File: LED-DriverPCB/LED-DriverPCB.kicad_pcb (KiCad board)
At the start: 4 copper layers, 246 x 144.3 mm, 51 parts, among them J1 Screw_Terminal_01x03, J12 Screw_Terminal_01x02, J13 Screw_Terminal_01x02, J14 Screw_Terminal_01x02, J15 Screw_Terminal_01x02, J16 Screw_Terminal_01x02, J17 Screw_Terminal_01x02, J18 Screw_Terminal_01x02, J19 Screw_Terminal_01x02, J2 Screw_Terminal_01x03, J20 Conn_ARM_SWD_TagConnect_TC2030, J3 Screw_Terminal_01x03, J4 Screw_Terminal_01x03, J5 Screw_Terminal_01x03, J6 Screw_Terminal_01x03, J7 Screw_Terminal_01x03, J8 Screw_Terminal_01x03, J9 USB_C_Receptacle_USB2.0_16P, U1 STM32F103RCTx, U2 TXB0108PW, U3 AMS1117-3.3, U4 USBLC6-2SC6, X1 8MHz

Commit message: Finalized layout
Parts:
- C1, C2: value C -> 10p
- moved J12 3.25 mm to (121.2, 99.0)
- moved J13 3.25 mm to (121.2, 111.6)
- moved J14 3.25 mm to (121.2, 124.2)
- moved J15 3.25 mm to (121.2, 136.8)
- moved J16 3.25 mm to (121.2, 149.5)
- moved J17 3.25 mm to (121.2, 162.1)
- moved J18 3.25 mm to (121.2, 174.7)
- moved J19 3.25 mm to (121.2, 187.3)
- moved J1 2.86 mm to (323.3, 200.1)
- moved J2 2.86 mm to (302.1, 200.1)
- moved J3 2.86 mm to (280.9, 200.1)
- moved J4 2.86 mm to (259.6, 200.1)
- moved J5 2.86 mm to (205.7, 200.1)
- moved J6 2.86 mm to (184.5, 200.1)
- moved J7 2.86 mm to (163.3, 200.1)
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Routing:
- net /STR6_PWR: track 100.1 -> 94.0 mm
- net /STR5_PWR: track 124.3 -> 118.2 mm
- net /STR4_PWR: track 178.6 -> 172.5 mm
- net /STR8_PWR: track 33.0 -> 26.8 mm
- net /STR7_PWR: track 66.7 -> 60.6 mm
- net /STR2_PWR: track 270.6 -> 264.5 mm
- net /STR3_PWR: track 240.6 -> 234.6 mm
- net /STR1_PWR: track 300.6 -> 294.6 mm
- net /STR8_DATA: track 130.6 -> 127.7 mm
- net /STR7_DATA: track 110.1 -> 107.2 mm
- net /STR6_DATA: track 89.5 -> 86.6 mm
- net /STR5_DATA: track 68.9 -> 66.0 mm
- net /STR4_DATA: track 69.4 -> 66.6 mm
- net /STR3_DATA: track 90.2 -> 87.3 mm
- net /STR2_DATA: track 110.8 -> 108.0 mm
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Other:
- board size 246 x 144.3 mm -> 244 x 142.3 mm
- board text added: "GND"
- board text added: "POWER 1"
- board text added: "POWER 2"
- board text added: "POWER 3"
- board text added: "POWER 4"
- board text added: "POWER 5"
- board text added: "POWER 6"
- board text added: "POWER 7"
- board text added: "POWER 8"
- board text added: "PWR"
- board text added: "STRIP 1"
- board text added: "STRIP 2"
- board text added: "STRIP 3"
- board text added: "STRIP 4"
- board text added: "STRIP 5"
- board text added: "STRIP 6"
- board text added: "STRIP 7"
- board text added: "STRIP 8"

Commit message: Finished PCB
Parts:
- added D1: LED, LED_SMD:LED_0603_1608Metric, F.Cu at (246.5, 143.1)
- added R6: 1k, Resistor_SMD:R_0402_1005Metric, F.Cu at (246.2, 144.7)
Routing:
- net +3.3V: track 114.8 -> 125.1 mm
- net Net-(D1-K): track 0.00 -> 1.61 mm
- net GND: track 49.7 -> 50.5 mm, vias 63 -> 62
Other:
- board text added: "06/25"
- board text added: "REV A"
- board text added: "Tim Short's Garage"
- board text added: "timshortsgarage.ca"

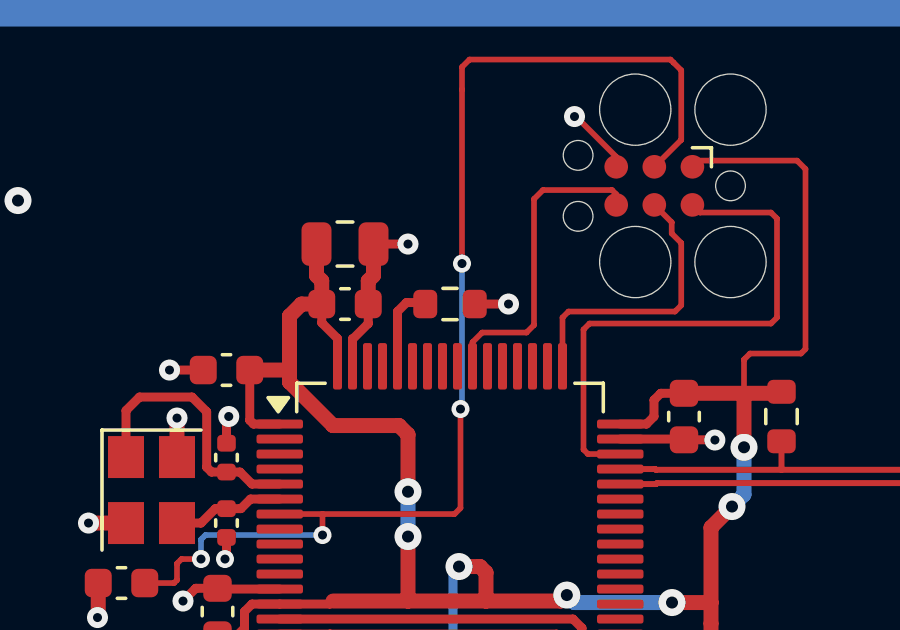
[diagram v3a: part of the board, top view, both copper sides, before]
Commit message: Changed MCU and level shifter
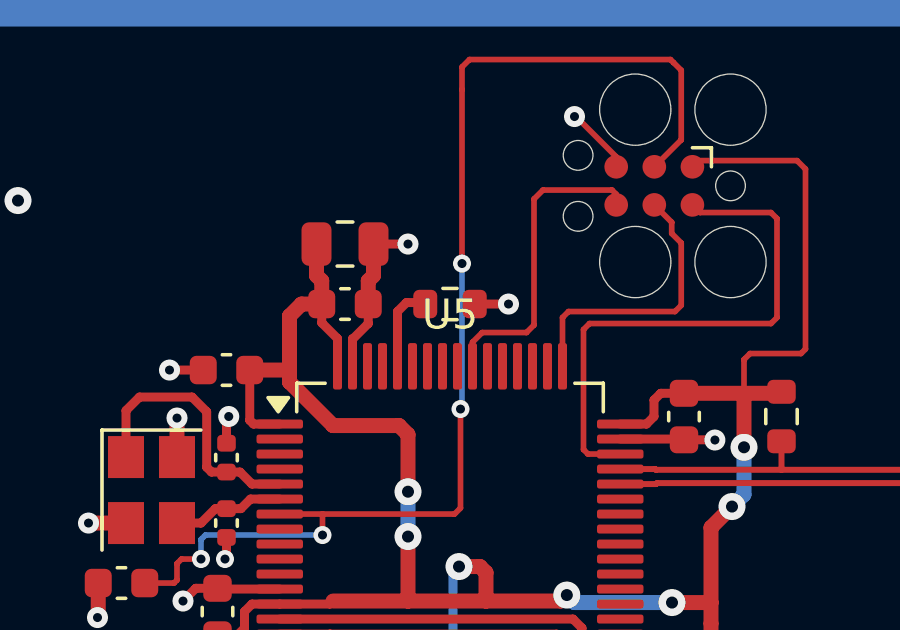
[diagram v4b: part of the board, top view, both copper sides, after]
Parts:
- removed U1: STM32F103RCTx, Package_QFP:LQFP-64_10x10mm_P0.5mm
- added U5: STM32F103RGTx, Package_QFP:LQFP-64_10x10mm_P0.5mm, F.Cu at (228.0, 139.5)

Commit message: fixed bugs
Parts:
- removed C13, C14: 100n, Capacitor_SMD:C_0603_1608Metric
- removed C15: 10u, Capacitor_SMD:C_0805_2012Metric
- removed U2: TXB0108PW, Package_SO:TSSOP-20_4.4x6.5mm_P0.65mm
- added C16: 100n, Capacitor_SMD:C_0603_1608Metric, F.Cu at (231.6, 152.0)
- added G***: LOGO, LOGO, F.Cu at (240.9, 104.2)
- added G***: LOGO, LOGO, F.Cu at (275.3, 114.9)
- added R10: 0R, Resistor_SMD:R_0603_1608Metric, F.Cu at (234.9, 157.7)
- added R11: 0R, Resistor_SMD:R_0603_1608Metric, F.Cu at (234.9, 159.5)
- added R12: 0R, Resistor_SMD:R_0603_1608Metric, F.Cu at (221.2, 154.0)
- added R13: 0R, Resistor_SMD:R_0603_1608Metric, F.Cu at (221.2, 155.8)
- added R14: 0R, Resistor_SMD:R_0603_1608Metric, F.Cu at (221.2, 157.7)
- added R15: 0R, Resistor_SMD:R_0603_1608Metric, F.Cu at (221.2, 159.5)
- added R7: 10k, Resistor_SMD:R_0603_1608Metric, F.Cu at (234.9, 152.1)
- added R8: 0R, Resistor_SMD:R_0603_1608Metric, F.Cu at (234.9, 154.0)
- added R9: 0R, Resistor_SMD:R_0603_1608Metric, F.Cu at (234.9, 155.8)
- added TP1: TestPoint, TestPoint:TestPoint_Pad_1.0x1.0mm, F.Cu at (216.9, 154.0)
- added TP2: TestPoint, TestPoint:TestPoint_Pad_1.0x1.0mm, F.Cu at (213.7, 155.8)
- added TP3: TestPoint, TestPoint:TestPoint_Pad_1.0x1.0mm, F.Cu at (210.4, 157.7)
- added TP4: TestPoint, TestPoint:TestPoint_Pad_1.0x1.0mm, F.Cu at (207.2, 159.5)
- added TP5: TestPoint, TestPoint:TestPoint_Pad_1.0x1.0mm, F.Cu at (248.1, 159.5)
- added TP6: TestPoint, TestPoint:TestPoint_Pad_1.0x1.0mm, F.Cu at (251.5, 157.7)
- added TP7: TestPoint, TestPoint:TestPoint_Pad_1.0x1.0mm, F.Cu at (254.9, 155.8)
- added TP8: TestPoint, TestPoint:TestPoint_Pad_1.0x1.0mm, F.Cu at (258.2, 154.0)
- added U1: 74AHCT244, Package_SO:TSSOP-20_4.4x6.5mm_P0.65mm, F.Cu at (228.0, 156.4)
- R4: value 50k -> 10k
- moved R4 3.28 mm to (221.2, 152.1), turned to 180 degrees
- moved C8 0.95 mm to (219.3, 142.0)
- moved C10 0.83 mm to (216.3, 141.0)
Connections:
- R4 pad 1: +3.3V -> Net-(U1-1OE)
- R4 pad 2: /SHIFTER_OE -> GND
- U5 pad 25: /PWM_TIM8_CH1 -> unconnected-(U5-PC5-Pad25)
- U5 pad 37: unconnected-(U5-PC6-Pad37) -> /PWM_TIM8_CH1
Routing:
- net VBUS: track 160.2 -> 137.5 mm
- net +3.3V: track 125.1 -> 108.2 mm, vias 10 -> 9
- net /PWM_TIM8_CH1: track 10.3 -> 24.7 mm, vias 0 -> 2
- net /STR5_DATA: track 66.0 -> 59.2 mm
- net /STR4_DATA: track 66.6 -> 60.0 mm
- net /PWM_TIM5_CH1: track 26.1 -> 19.8 mm
- net /PWM_TIM3_CH1: track 12.3 -> 17.5 mm, vias 2 -> 0
- net /PWM_TIM5_CH2: track 25.3 -> 20.1 mm
- net /PWM_TIM5_CH4: track 17.7 -> 22.7 mm, vias 2 -> 0
- net Net-(U1-2OE): track 0.00 -> 4.62 mm
- net /STR6_DATA: track 86.6 -> 82.3 mm
- net Net-(U1-1OE): track 0.00 -> 4.26 mm
- net /STR3_DATA: track 87.3 -> 83.1 mm
- net /PWM_TIM3_CH3: track 9.18 -> 13.4 mm, vias 2 -> 0
- net /2Y3_RES: track 0.00 -> 3.50 mm
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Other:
- board text added: "07/25"
- board text added: "REV B"
- board text removed: "06/25"
- board text removed: "REV A"

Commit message: Small changes
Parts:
- added G***: LOGO, LOGO, F.Cu at (205.7, 131.7)
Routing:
- net +3.3V: track 108.2 -> 109.6 mm

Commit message: Fixed issues
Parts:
- moved TP1 41.3 mm to (216.9, 154.0)
- moved TP8 41.3 mm to (258.2, 154.0)
- moved TP2 41.2 mm to (213.7, 155.8)
- moved TP7 41.2 mm to (254.9, 155.8)
- moved TP3 41.1 mm to (210.4, 157.7)
- moved TP6 41.1 mm to (251.5, 157.7)
- moved TP4 40.9 mm to (207.2, 159.5)
- moved TP5 40.9 mm to (248.1, 159.5)
- renumbered TP8 to TP1, TP7 to TP2, TP6 to TP3, TP5 to TP4, TP4 to TP5, TP3 to TP6, TP2 to TP7, TP1 to TP8
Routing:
- net VBUS: track 137.5 -> 146.1 mm
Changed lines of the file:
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@@
 			)
 		)
+		(property "JLCPCB Part #" "C21189"
+			(at 0 0 0)
+			(unlocked yes)
+			(layer "F.Fab")
+			(hide yes)
+			(effects
+				(font
+					(size 1 1)
+					(thickness 0.15)
+				)
+			)
+		)
 		(property ki_fp_filters "R_*")
 		(sheetname "/")
@@
 			)
 		)
+		(property "JLCPCB Part #" " C25804"
+			(at 0 0 180)
+			(unlocked yes)
+			(layer "F.Fab")
+			(hide yes)
+			(effects
+				(font
+					(size 1 1)
+					(thickness 0.15)
+				)
+			)
+		)
 		(property ki_fp_filters "R_*")
 		(sheetname "/")
@@
 			)
 		)
+		(property "JLCPCB Part #" "C484743"
+			(at 0 0 0)
+			(unlocked yes)
+			(layer "F.Fab")
+			(hide yes)
+			(effects
+				(font
+					(size 1 1)
+					(thickness 0.15)
+				)
+			)
+		)
 		(property ki_fp_filters "TSSOP*4.4x6.5mm*P0.65mm* SSOP*4.4x6.5mm*P0.65mm*")
 		(sheetname "/")
@@
 			)
 		)
+		(property "JLCPCB Part #" "C21189"
+			(at 0 0 180)
+			(unlocked yes)
+			(layer "F.Fab")
+			(hide yes)
+			(effects
+				(font
+					(size 1 1)
+					(thickness 0.15)
+				)
+			)
+		)
 		(property ki_fp_filters "R_*")
 		(sheetname "/")
@@
 	(footprint "TestPoint:TestPoint_Pad_1.0x1.0mm"
 		(layer "F.Cu")
-		(at 216.879 153.959)
+		(at 258.229 153.959)
 		(descr "SMD rectangular pad as test Point, square 1.0mm side length")
 		(tags "test point SMD pad rectangle square")
-		(property "Reference" "TP1"
+		(property "Reference" "TP8"
 			(at -2.85 -0.925 0)
 			(layer "F.SilkS")
@@
 	(footprint "TestPoint:TestPoint_Pad_1.0x1.0mm"
 		(layer "F.Cu")
-		(at 251.495667 157.659)
+		(at 210.445667 157.659)
 		(descr "SMD rectangular pad as test Point, square 1.0mm side length")
 		(tags "test point SMD pad rectangle square")
-		(property "Reference" "TP6"
+		(property "Reference" "TP3"
 			(at -2.733333 -0.833333 0)
 			(layer "F.SilkS")
@@
 			)
 		)
+		(property "JLCPCB Part #" "C21189"
+			(at 0 0 180)
+			(unlocked yes)
+			(layer "F.Fab")
+			(hide yes)
+			(effects
+				(font
+					(size 1 1)
+					(thickness 0.15)
+				)
+			)
+		)
 		(property ki_fp_filters "R_*")
 		(sheetname "/")
@@
 	(footprint "TestPoint:TestPoint_Pad_1.0x1.0mm"
 		(layer "F.Cu")
-		(at 213.662333 155.809)
+		(at 254.862333 155.809)
 		(descr "SMD rectangular pad as test Point, square 1.0mm side length")
 		(tags "test point SMD pad rectangle square")
-		(property "Reference" "TP2"
+		(property "Reference" "TP7"
 			(at -2.833333 -0.908333 0)
 			(layer "F.SilkS")
@@
 			)
 		)
+		(property "JLCPCB Part #" "C21189"
+			(at 0 0 0)
+			(unlocked yes)
+			(layer "F.Fab")
+			(hide yes)
+			(effects
+				(font
+					(size 1 1)
+					(thickness 0.15)
+				)
+			)
+		)
 		(property ki_fp_filters "R_*")
 		(sheetname "/")
@@
 			)
 		)
+		(property "JLCPCB Part #" "C21189"
+			(at 0 0 180)
+			(unlocked yes)
+			(layer "F.Fab")
+			(hide yes)
+			(effects
+				(font
+					(size 1 1)
+					(thickness 0.15)
+				)
+			)
+		)
 		(property ki_fp_filters "R_*")
 		(sheetname "/")
@@
 	(footprint "TestPoint:TestPoint_Pad_1.0x1.0mm"
 		(layer "F.Cu")
-		(at 258.229 153.959)
+		(at 216.879 153.959)
 		(descr "SMD rectangular pad as test Point, square 1.0mm side length")
 		(tags "test point SMD pad rectangle square")
-		(property "Reference" "TP8"
+		(property "Reference" "TP1"
 			(at -2.8 -0.85 0)
 			(layer "F.SilkS")
@@
 			)
 		)
+		(property "JLCPCB Part #" " C25804"
+			(at 0 0 0)
+			(unlocked yes)
+			(layer "F.Fab")
+			(hide yes)
+			(effects
+				(font
+					(size 1 1)
+					(thickness 0.15)
+				)
+			)
+		)
 		(property ki_fp_filters "R_*")
 		(sheetname "/")
@@
 			)
 		)
-		(property "JLCPCB Part #" "C5184132"
+		(property "JLCPCB Part #" " C25804"
 			(at 0 0 180)
 			(unlocked yes)
@@
 			)
 		)
+		(property "JLCPCB Part #" "C1590"
+			(at 0 0 180)
+			(unlocked yes)
+			(layer "F.Fab")
+			(hide yes)
+			(effects
+				(font
+					(size 1 1)
+					(thickness 0.15)
+				)
+			)
+		)
 		(property ki_fp_filters "C_*")
 		(sheetname "/")
@@
 			)
 		)
+		(property "JLCPCB Part #" "C21189"
+			(at 0 0 0)
+			(unlocked yes)
+			(layer "F.Fab")
+			(hide yes)
+			(effects
+				(font
+					(size 1 1)
+					(thickness 0.15)
+				)
+			)
+		)
 		(property ki_fp_filters "R_*")
 		(sheetname "/")
@@
 	(footprint "TestPoint:TestPoint_Pad_1.0x1.0mm"
 		(layer "F.Cu")
-		(at 254.862333 155.809)
+		(at 213.662333 155.809)
 		(descr "SMD rectangular pad as test Point, square 1.0mm side length")
 		(tags "test point SMD pad rectangle square")
-		(property "Reference" "TP7"
+		(property "Reference" "TP2"
 			(at -2.766667 -0.866667 0)
 			(layer "F.SilkS")
@@
 	(footprint "TestPoint:TestPoint_Pad_1.0x1.0mm"
 		(layer "F.Cu")
-		(at 207.229 159.509)
+		(at 248.104 159.509)
 		(descr "SMD rectangular pad as test Point, square 1.0mm side length")
 		(tags "test point SMD pad rectangle square")
-		(property "Reference" "TP4"
+		(property "Reference" "TP5"
 			(at -2.8 -0.875 0)
 			(layer "F.SilkS")
@@
 	(footprint "TestPoint:TestPoint_Pad_1.0x1.0mm"
 		(layer "F.Cu")
-		(at 210.445667 157.659)
+		(at 251.495667 157.659)
 		(descr "SMD rectangular pad as test Point, square 1.0mm side length")
 		(tags "test point SMD pad rectangle square")
-		(property "Reference" "TP3"
+		(property "Reference" "TP6"
 			(at -2.816667 -0.891667 0)
 			(layer "F.SilkS")
@@
 			)
 		)
+		(property "JLCPCB Part #" "C21189"
+			(at 0 0 180)
+			(unlocked yes)
+			(layer "F.Fab")
+			(hide yes)
+			(effects
+				(font
+					(size 1 1)
+					(thickness 0.15)
+				)
+			)
+		)
 		(property ki_fp_filters "R_*")
 		(sheetname "/")
@@
 			)
 		)
+		(property "JLCPCB Part #" "C21189"
+			(at 0 0 180)
+			(unlocked yes)
+			(layer "F.Fab")
+			(hide yes)
+			(effects
+				(font
+					(size 1 1)
+					(thickness 0.15)
+				)
+			)
+		)
 		(property ki_fp_filters "R_*")
 		(sheetname "/")
@@
 	(footprint "TestPoint:TestPoint_Pad_1.0x1.0mm"
 		(layer "F.Cu")
-		(at 248.104 159.509)
+		(at 207.229 159.509)
 		(descr "SMD rectangular pad as test Point, square 1.0mm side length")
 		(tags "test point SMD pad rectangle square")
-		(property "Reference" "TP5"
+		(property "Reference" "TP4"
 			(at -2.7 -0.8 0)
 			(layer "F.SilkS")
@@
 	)
 	(segment
+		(start 232.404 151.959)
+		(end 232.404 150.959)
+		(width 0.5)
+		(layer "F.Cu")
+		(net 73)
+	)
+	(segment
 		(start 232.404 153.234)
 		(end 232.404 151.959)
@@
 	)
 	(segment
+		(start 234.779 150.659)
+		(end 234.979 150.459)
+		(width 0.5)
+		(layer "F.Cu")
+		(net 73)
+	)
+	(segment
 		(start 344.160251 144.441)
 		(end 344.660251 143.941)
@@
 	)
 	(segment
-		(start 238.379 151.041)
-		(end 239.029 151.041)
+		(start 241.029 151.491)
+		(end 243.611 151.491)
 		(width 0.5)
 		(layer "F.Cu")
@@
 	)
 	(segment
-		(start 241.029 151.491)
-		(end 243.611 151.491)
+		(start 239.761 151.491)
+		(end 241.029 151.491)
 		(width 0.5)
 		(layer "F.Cu")
@@
 	)
 	(segment
+		(start 234.979 150.034)
+		(end 235.221 149.792)
+		(width 0.5)
+		(layer "F.Cu")
+		(net 73)
+	)
+	(segment
 		(start 335.084251 138.5379)
 		(end 335.631151 137.991)
@@
 	)
 	(segment
+		(start 237.186 151.041)
+		(end 238.379 151.041)
+		(width 0.5)
+		(layer "F.Cu")
+		(net 73)
+	)
+	(segment
 		(start 333.829 152.159)
 		(end 335.084251 150.903749)
@@
 	)
 	(segment
+		(start 236.929 150.784)
+		(end 237.186 151.041)
+		(width 0.5)
+		(layer "F.Cu")
+		(net 73)
+	)
+	(segment
 		(start 335.084251 144.441)
 		(end 335.084251 138.5379)
@@
 	)
 	(segment
+		(start 239.311 151.041)
+		(end 239.761 151.491)
+		(width 0.5)
+		(layer "F.Cu")
+		(net 73)
+	)
+	(segment
+		(start 234.979 150.459)
+		(end 234.979 150.034)
+		(width 0.5)
+		(layer "F.Cu")
+		(net 73)
+	)
+	(segment
 		(start 243.611 151.491)
 		(end 244.279 152.159)
@@
 	)
 	(segment
+		(start 236.929 150.092)
+		(end 236.929 150.784)
+		(width 0.5)
+		(layer "F.Cu")
+		(net 73)
+	)
+	(segment
 		(start 342.873532 140.441)
 		(end 342.015251 140.441)
@@
 	)
 	(segment
-		(start 344.660251 143.941)
-		(end 344.660251 139.291)
+		(start 232.404 150.959)
+		(end 232.704 150.659)
 		(width 0.5)
 		(layer "F.Cu")
@@
 	)
 	(segment
-		(start 239.479 151.491)
-		(end 241.029 151.491)
+		(start 344.660251 143.941)
+		(end 344.660251 139.291)
 		(width 0.5)
 		(layer "F.Cu")
@@
 	)
 	(segment
-		(start 239.029 151.041)
-		(end 239.479 151.491)
+		(start 342.015251 135.541)
+		(end 342.873532 135.541)
+		(width 0.3)
+		(layer "F.Cu")
+		(net 73)
+	)
+	(segment
+		(start 235.221 149.792)
+		(end 236.629 149.792)
 		(width 0.5)
 		(layer "F.Cu")
@@
 	)
 	(segment
-		(start 342.015251 135.541)
-		(end 342.873532 135.541)
-		(width 0.3)
+		(start 238.379 151.041)
+		(end 239.311 151.041)
+		(width 0.5)
 		(layer "F.Cu")
 		(net 73)
@@
 		(width 0.5)
 		(layer "F.Cu")
+		(net 73)
+	)
+	(segment
+		(start 236.629 149.792)
+		(end 236.929 150.092)
+		(width 0.5)
+		(layer "F.Cu")
+		(net 73)
+	)
+	(segment
+		(start 232.704 150.659)
+		(end 234.779 150.659)
+		(width 0.5)
+		(layer "F.Cu")

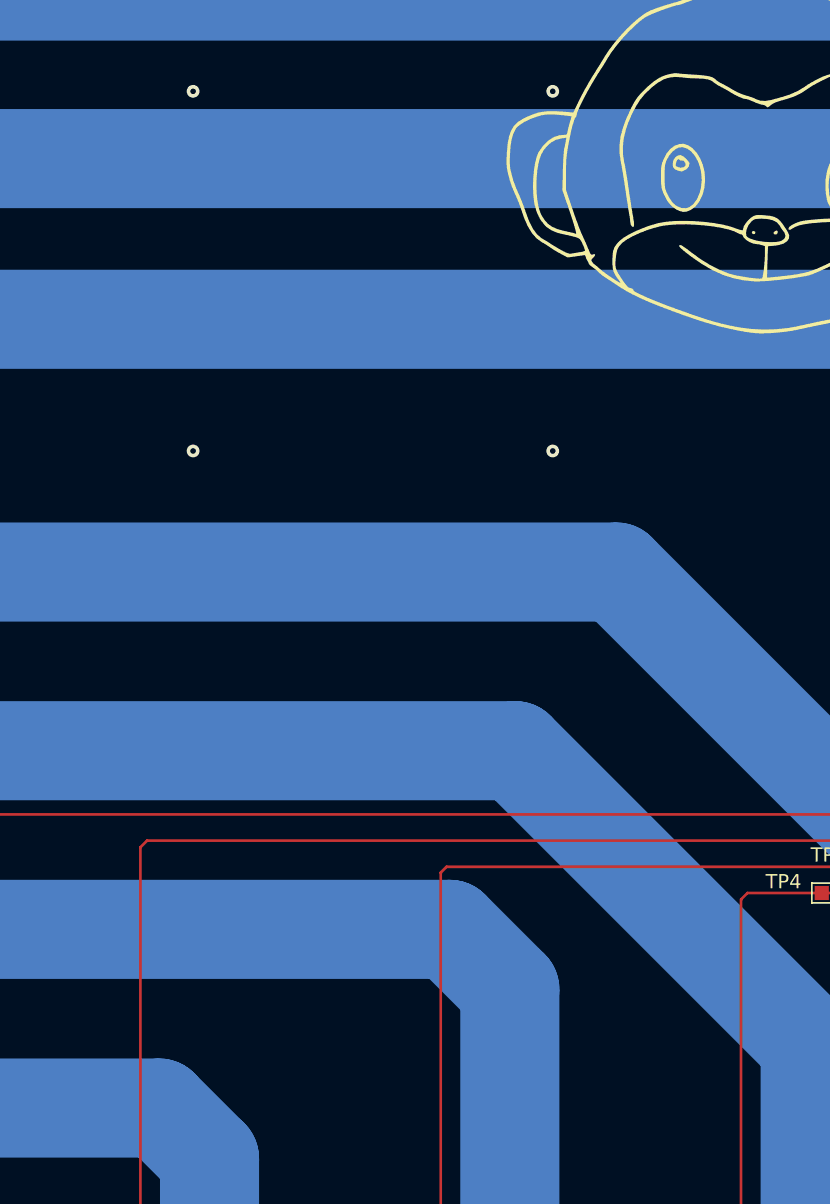
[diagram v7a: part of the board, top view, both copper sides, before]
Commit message: Added garage logo
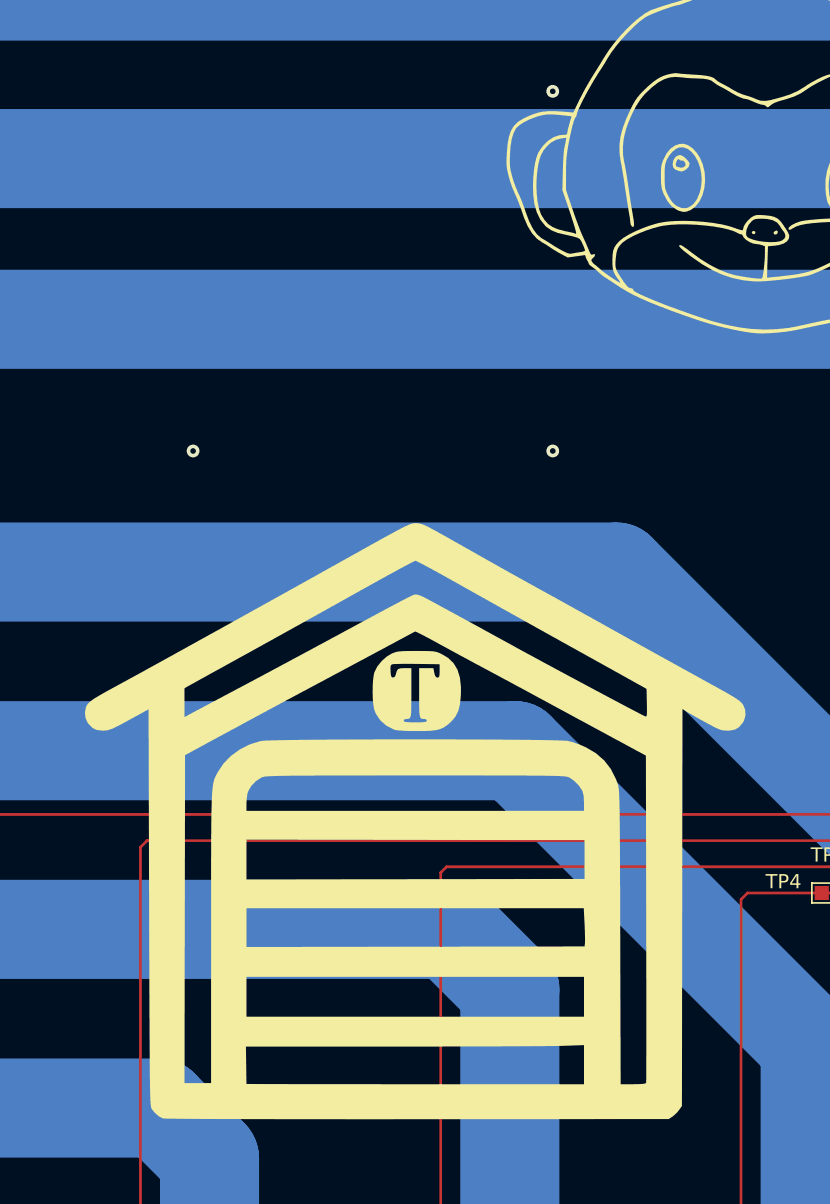
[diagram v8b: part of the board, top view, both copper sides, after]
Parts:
- added G***: LOGO, LOGO, F.Cu at (178.5, 155.6)
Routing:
- net GND: vias 56 -> 55
